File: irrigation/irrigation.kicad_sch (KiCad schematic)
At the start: 37 parts, among them J1 24V Jmp, J10 24V, J11 25%, J12 50%, J13 75%, J14 100%, J15 100%, J16 100%, J17 Pump, J2 Power, J3 Power, J4 Power, J5 Power, J6 Power, J7 Power, J8 0V Jmp, J9 Empty, K1 PLC-RPT-24DC/21, K2 PLC-RPT-24DC/21, M1 Pump, SW1 Well Empty, SW2 100% Full, SW3 25% Full, SW4 50% Full, SW5 75% Full, U1 MPPT-Charger

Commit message: Attempting to organize
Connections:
- net at J10.: now also J15.; no longer J14.
- net at J16.: now also J15.; no longer J14.
- new net: J10., J14.
- new net: J14., J16.
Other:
- note added: "Front-Panel LEDs"
- moved on the sheet: D1, D2, D3, D4, D5, D6, J10, J11, J12, J13, J14, J15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

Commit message: Organization
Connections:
- net at J10.: now also J15.; no longer J14.
- net at J16.: now also J15.; no longer J14.
- new net: J10., J14.
- new net: J14., J16.
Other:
- moved on the sheet: D1, D2, D3, D4, D5, D6, J10, J11, J12, J13, J14, J15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

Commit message: Organization
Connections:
- net at J10.: now also J15.; no longer J14.
- net at J16.: now also J15.; no longer J14.
- new net: J10., J14.
- new net: J14., J16.
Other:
- company: (none) -> Catsle
- title: (none) -> Irrigation Phase 1
- moved on the sheet: K1, K2
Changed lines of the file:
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@@
 	(generator "eeschema")
 	(generator_version "9.0")
-	(paper "A4")
+	(paper "A")
+	(title_block
+		(title "Irrigation Phase 1")
+		(date "2025-04-03")
+		(rev "1")
+		(company "Catsle")
+	)
 	(rectangle
 		(start 15.24 140.97)
@@
 	)
 	(no_connect
-		(at 187.96 60.96)
+		(at 185.42 60.96)
 	)
 	(no_connect
@@
 	(wire
 		(pts
-			(xy 142.24 140.97) (xy 151.13 140.97)
+			(xy 142.24 140.97) (xy 147.32 140.97)
 		)
 		(stroke
@@
 	(wire
 		(pts
-			(xy 227.33 64.77) (xy 246.38 64.77)
+			(xy 227.33 64.77) (xy 236.22 64.77)
 		)
 		(stroke
@@
 	(wire
 		(pts
-			(xy 227.33 152.4) (xy 246.38 152.4)
+			(xy 227.33 152.4) (xy 236.22 152.4)
 		)
 		(stroke
@@
 	(wire
 		(pts
-			(xy 110.49 29.21) (xy 208.28 29.21)
+			(xy 110.49 29.21) (xy 203.2 29.21)
 		)
 		(stroke
@@
 	(wire
 		(pts
-			(xy 227.33 97.79) (xy 246.38 97.79)
+			(xy 227.33 97.79) (xy 236.22 97.79)
 		)
 		(stroke
@@
 	(wire
 		(pts
-			(xy 227.33 81.28) (xy 246.38 81.28)
+			(xy 227.33 81.28) (xy 236.22 81.28)
 		)
 		(stroke
@@
 	(wire
 		(pts
-			(xy 166.37 143.51) (xy 170.18 143.51)
+			(xy 162.56 143.51) (xy 166.37 143.51)
 		)
 		(stroke
@@
 	(wire
 		(pts
-			(xy 187.96 55.88) (xy 208.28 55.88)
+			(xy 185.42 55.88) (xy 203.2 55.88)
 		)
 		(stroke
@@
 	(wire
 		(pts
-			(xy 170.18 58.42) (xy 172.72 58.42)
+			(xy 166.37 58.42) (xy 170.18 58.42)
 		)
 		(stroke
@@
 	(wire
 		(pts
-			(xy 227.33 138.43) (xy 246.38 138.43)
+			(xy 227.33 138.43) (xy 236.22 138.43)
 		)
 		(stroke
@@
 	(wire
 		(pts
-			(xy 110.49 48.26) (xy 172.72 48.26)
+			(xy 110.49 48.26) (xy 170.18 48.26)
 		)
 		(stroke
@@
 	(wire
 		(pts
-			(xy 204.47 152.4) (xy 219.71 152.4)
+			(xy 212.09 152.4) (xy 219.71 152.4)
 		)
 		(stroke
@@
 	(wire
 		(pts
-			(xy 110.49 130.81) (xy 151.13 130.81)
+			(xy 110.49 130.81) (xy 147.32 130.81)
 		)
 		(stroke
@@
 	(wire
 		(pts
-			(xy 187.96 48.26) (xy 194.31 48.26)
+			(xy 185.42 48.26) (xy 189.23 48.26)
 		)
 		(stroke
@@
 	(wire
 		(pts
-			(xy 166.37 130.81) (xy 176.53 130.81)
+			(xy 162.56 130.81) (xy 172.72 130.81)
 		)
 		(stroke
@@
 	(wire
 		(pts
-			(xy 208.28 29.21) (xy 208.28 55.88)
+			(xy 203.2 29.21) (xy 203.2 55.88)
 		)
 		(stroke
@@
 	(wire
 		(pts
-			(xy 227.33 114.3) (xy 246.38 114.3)
+			(xy 227.33 114.3) (xy 236.22 114.3)
 		)
 		(stroke
@@
 	(wire
 		(pts
-			(xy 170.18 58.42) (xy 170.18 143.51)
+			(xy 166.37 58.42) (xy 166.37 143.51)
 		)
 		(stroke
@@
 	(wire
 		(pts
-			(xy 166.37 138.43) (xy 219.71 138.43)
+			(xy 162.56 138.43) (xy 219.71 138.43)
 		)
 		(stroke
@@
 	)
 	(label "8"
-		(at 167.64 143.51 0)
+		(at 163.83 143.51 0)
 		(effects
 			(font
@@
 	)
 	(label "19"
-		(at 173.99 130.81 0)
+		(at 170.18 130.81 0)
 		(effects
 			(font
@@
 	)
 	(label "27"
-		(at 167.64 138.43 0)
+		(at 163.83 138.43 0)
 		(effects
 			(font
@@
 	)
 	(label "25"
-		(at 149.86 130.81 180)
+		(at 146.05 130.81 180)
 		(effects
 			(font
@@
 	)
 	(label "26"
-		(at 189.23 55.88 0)
+		(at 186.69 55.88 0)
 		(effects
 			(font
@@
 	)
 	(label "24"
-		(at 171.45 48.26 180)
+		(at 168.91 48.26 180)
 		(effects
 			(font
@@
 	)
 	(label "14"
-		(at 189.23 48.26 0)
+		(at 186.69 48.26 0)
 		(effects
 			(font
@@
 	)
 	(label "8"
-		(at 171.45 58.42 180)
+		(at 168.91 58.42 180)
 		(effects
 			(font
@@
 	)
 	(label "20"
-		(at 147.32 140.97 180)
+		(at 146.05 140.97 180)
 		(effects
 			(font
@@
 	(global_label "100% Out"
 		(shape input)
-		(at 194.31 48.26 0)
+		(at 189.23 48.26 0)
 		(fields_autoplaced yes)
 		(effects
@@
 		)
 		(property "Intersheetrefs" "${INTERSHEET_REFS}"
-			(at 206.5479 48.26 0)
+			(at 201.4679 48.26 0)
 			(effects
 				(font
@@
 	(global_label "Empty Out"
 		(shape input)
-		(at 176.53 130.81 0)
+		(at 172.72 130.81 0)
 		(fields_autoplaced yes)
 		(effects
@@
 		)
 		(property "Intersheetrefs" "${INTERSHEET_REFS}"
-			(at 189.3726 130.81 0)
+			(at 185.5626 130.81 0)
 			(effects
 				(font
@@
 	(global_label "75% Out"
 		(shape input)
-		(at 246.38 81.28 0)
+		(at 236.22 81.28 0)
 		(fields_autoplaced yes)
 		(effects
@@
 		)
 		(property "Intersheetrefs" "${INTERSHEET_REFS}"
-			(at 257.4084 81.28 0)
+			(at 247.2484 81.28 0)
 			(effects
 				(font
@@
 	(global_label "25% Out"
 		(shape input)
-		(at 246.38 114.3 0)
+		(at 236.22 114.3 0)
 		(fields_autoplaced yes)
 		(effects
@@
 		)
 		(property "Intersheetrefs" "${INTERSHEET_REFS}"
-			(at 257.4084 114.3 0)
+			(at 247.2484 114.3 0)
 			(effects
 				(font
@@
 	(global_label "50% Out"
 		(shape input)
-		(at 246.38 97.79 0)
+		(at 236.22 97.79 0)
 		(fields_autoplaced yes)
 		(effects
@@
 		)
 		(property "Intersheetrefs" "${INTERSHEET_REFS}"
-			(at 257.4084 97.79 0)
+			(at 247.2484 97.79 0)
 			(effects
 				(font
@@
 	(global_label "100% LED Out"
 		(shape input)
-		(at 246.38 64.77 0)
+		(at 236.22 64.77 0)
 		(fields_autoplaced yes)
 		(effects
@@
 		)
 		(property "Intersheetrefs" "${INTERSHEET_REFS}"
-			(at 263.0326 64.77 0)
+			(at 252.8726 64.77 0)
 			(effects
 				(font
@@
 	(global_label "Power In"
 		(shape input)
-		(at 204.47 152.4 180)
+		(at 212.09 152.4 180)
 		(fields_autoplaced yes)
 		(effects
@@
 		)
 		(property "Intersheetrefs" "${INTERSHEET_REFS}"
-			(at 193.1391 152.4 0)
+			(at 200.7591 152.4 0)
 			(effects
 				(font
@@
 	(global_label "Empty LED Out"
 		(shape input)
-		(at 246.38 138.43 0)
+		(at 236.22 138.43 0)
 		(fields_autoplaced yes)
 		(effects
@@
 		)
 		(property "Intersheetrefs" "${INTERSHEET_REFS}"
-			(at 263.6373 138.43 0)
+			(at 253.4773 138.43 0)
 			(effects
 				(font
@@
 	(global_label "Power Out"
 		(shape input)
-		(at 246.38 152.4 0)
+		(at 236.22 152.4 0)
 		(fields_autoplaced yes)
 		(effects
@@
 		)
 		(property "Intersheetrefs" "${INTERSHEET_REFS}"
-			(at 259.1623 152.4 0)
+			(at 249.0023 152.4 0)
 			(effects
 				(font
@@
 	(symbol
 		(lib_id "Phoenix Contact:PLC-RPT-24DC/21")
-		(at 180.34 53.34 270)
+		(at 177.8 53.34 270)
 		(unit 1)
 		(exclude_from_sim no)
@@
 		(fields_autoplaced yes)
 		(property "Reference" "K2"
-			(at 180.34 38.1 90)
+			(at 177.8 38.1 90)
 			(effects
 				(font
@@
 		)
 		(property "Value" "PLC-RPT-24DC/21"
-			(at 180.34 40.64 90)
+			(at 177.8 40.64 90)
 			(effects
 				(font
@@
 		)
 		(property "Footprint" ""
-			(at 179.324 82.296 0)
+			(at 176.784 82.296 0)
 			(effects
 				(font
@@
 		)
 		(property "Datasheet" "https://www.mouser.com/ProductDetail/Phoenix-Contact/2900299?qs=yDWYzLgaxI2Ztu%2F0JMLp4g%3D%3D"
-			(at 180.34 53.34 0)
+			(at 177.8 53.34 0)
 			(effects
 				(font
@@
 		)
 		(property "Description" "PLC-RPT- 24DC/21 - Relay module"
-			(at 180.34 53.34 0)
+			(at 177.8 53.34 0)
 			(effects
 				(font
@@
 	(symbol
 		(lib_id "Phoenix Contact:PLC-RPT-24DC/21")
-		(at 158.75 135.89 270)
+		(at 154.94 135.89 270)
 		(unit 1)
 		(exclude_from_sim no)
@@
 		(fields_autoplaced yes)
 		(property "Reference" "K1"
-			(at 158.75 120.65 90)
+			(at 154.94 120.65 90)
 			(effects
 				(font
@@
 		)
 		(property "Value" "PLC-RPT-24DC/21"
-			(at 158.75 123.19 90)
+			(at 154.94 123.19 90)
 			(effects
 				(font
@@
 		)
 		(property "Footprint" ""
-			(at 157.734 164.846 0)
+			(at 153.924 164.846 0)
 			(effects
 				(font
@@
 		)
 		(property "Datasheet" "https://www.mouser.com/ProductDetail/Phoenix-Contact/2900299?qs=yDWYzLgaxI2Ztu%2F0JMLp4g%3D%3D"
-			(at 158.75 135.89 0)
+			(at 154.94 135.89 0)
 			(effects
 				(font
@@
 		)
 		(property "Description" "PLC-RPT- 24DC/21 - Relay module"
-			(at 158.75 135.89 0)
+			(at 154.94 135.89 0)
 			(effects
 				(font

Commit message: Organized.
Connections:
- net 8 is gone; now on net Empty Out: K1.14, K2.11
- net at J10.: now also J15.; no longer J14.
- net at J16.: now also J15.; no longer J14.
- new net: J10., J14.
- new net: J14., J16.
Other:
- note added: "Pump Control"
- moved on the sheet: D1, D2, D3, D4, D5, D6, K1, K2

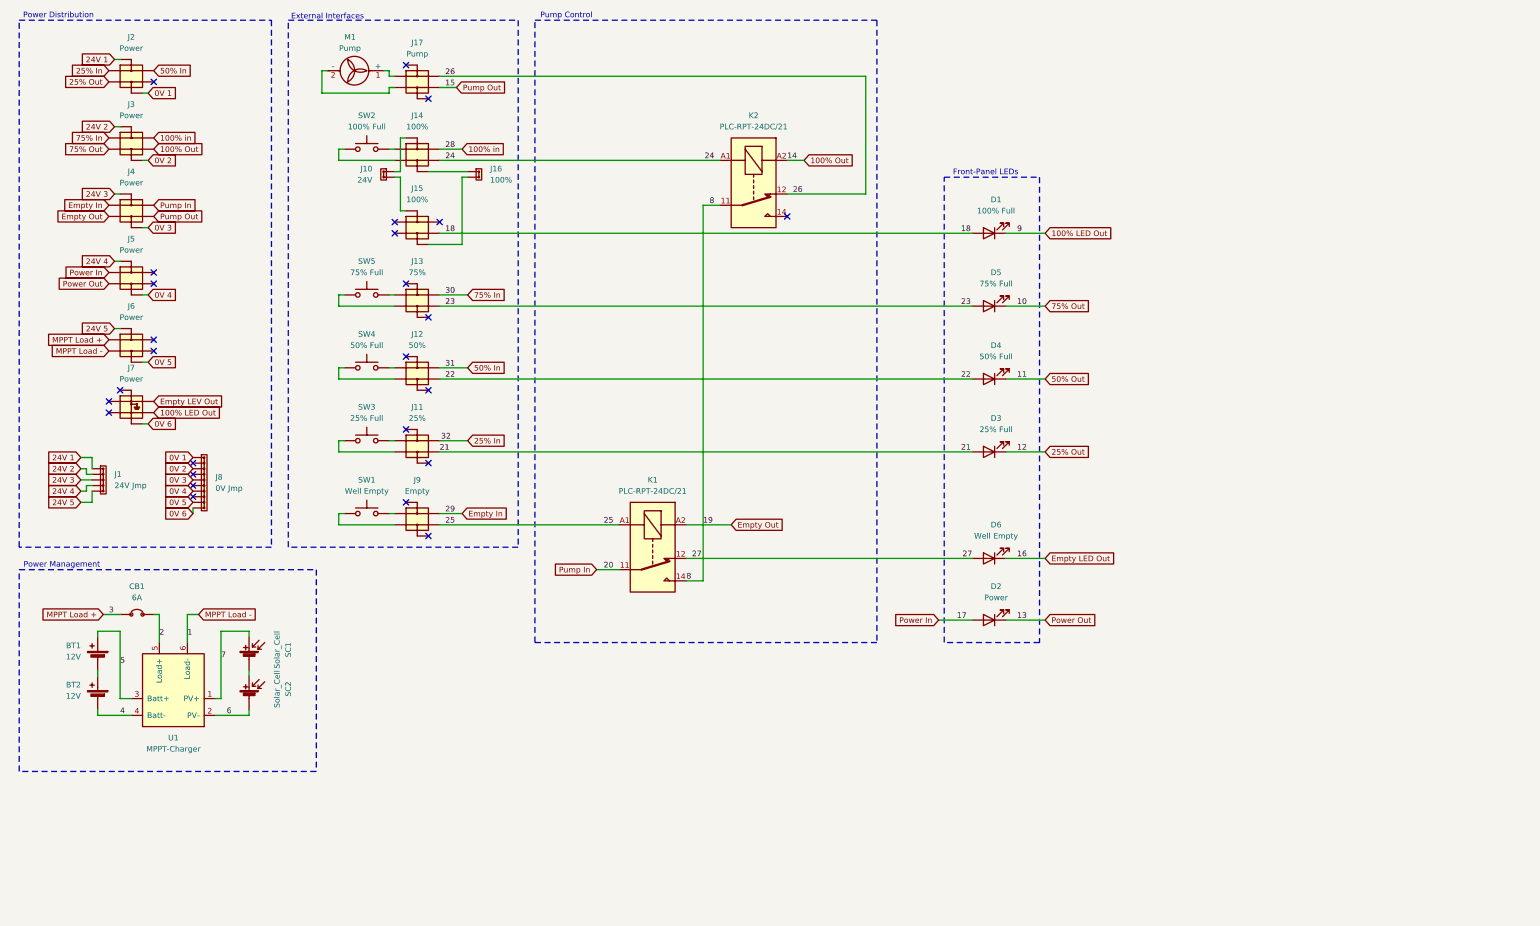
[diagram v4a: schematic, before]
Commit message: Working on adding switches and another pump
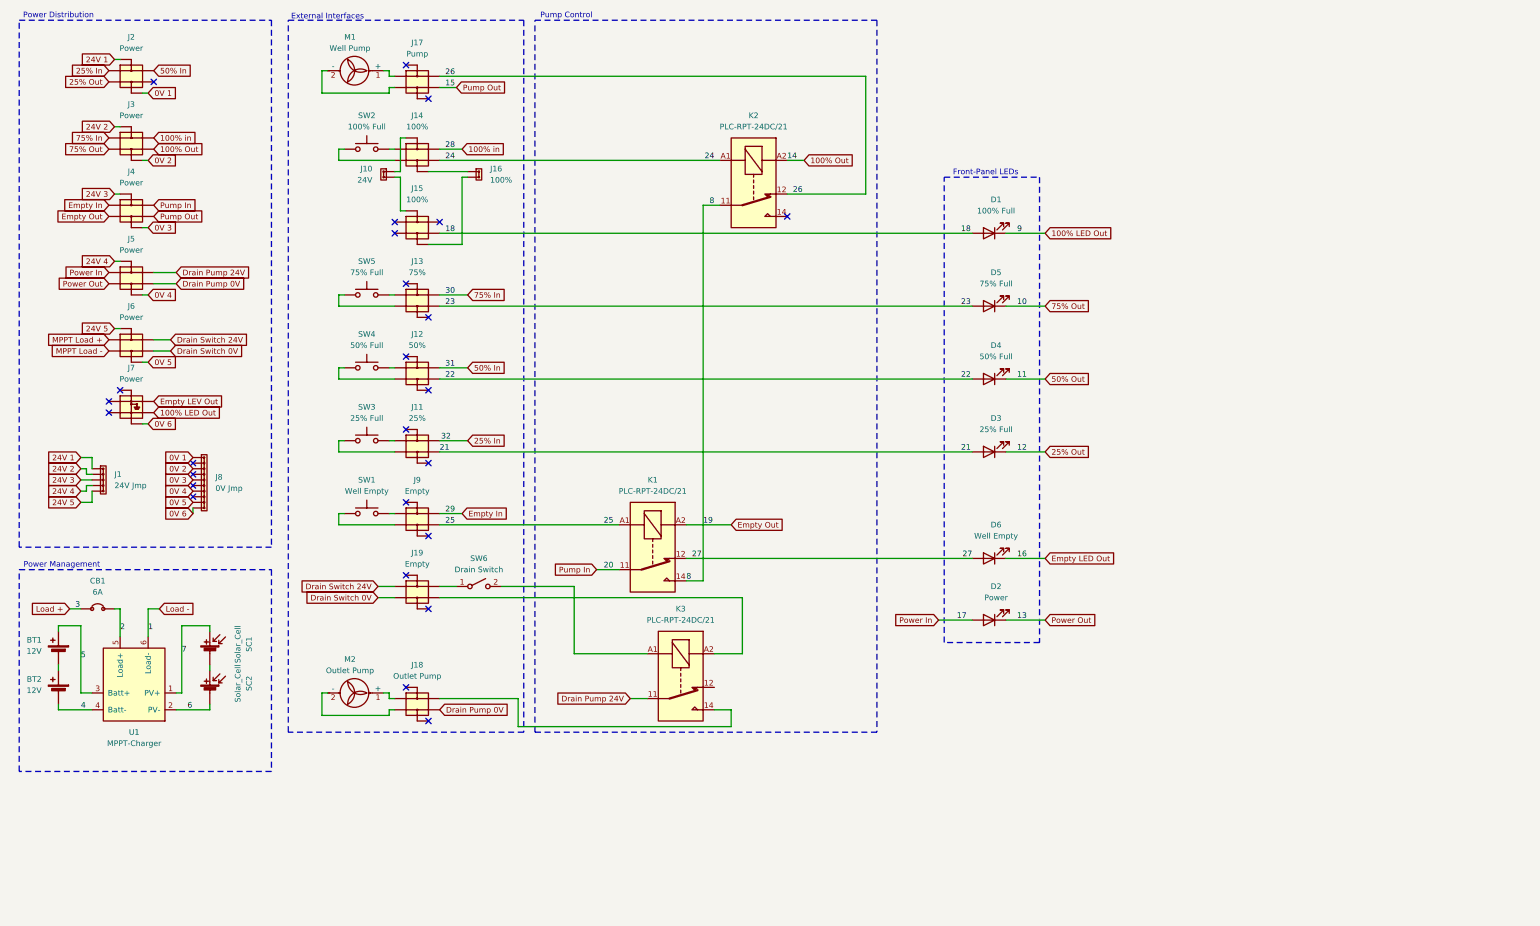
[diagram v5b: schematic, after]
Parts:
- added J18: Outlet Pump, symbol Phoenix Contact:PTTB_2,5-L/N_3210994
- added J19: Empty, symbol Phoenix Contact:PTTB_2,5-L/N_3210994
- added K3: PLC-RPT-24DC/21, symbol Phoenix Contact:PLC-RPT-24DC/21
- added M2: Outlet Pump, symbol Irrigation:Pump
- added SW6: Drain Switch, symbol Irrigation:Toggle Switch
- M1: value Pump -> Well Pump
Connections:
- net MPPT Load +: no longer CB1.
- net MPPT Load -: no longer U1.6 (Load-)
- net at J10.: now also J15.; no longer J14.
- net at J16.: now also J15.; no longer J14.
- new net: J10., J14.
- new net: J14., J16.
- new net: J18., K3.14
- new net: K3.A1, SW6.2 (B)
- new net: J19., K3.A2
- new net: J18., M2.1 (+)
- new net: J18., M2.2 (-)
- new net: J19., SW6.1 (A)
- new net Drain Pump 0V: J18., J5.
- new net Drain Pump 24V: J5., K3.11
- new net Drain Switch 0V: J19., J6.
- new net Drain Switch 24V: J19., J6.
- new net Load +: CB1.
- new net Load -: U1.6 (Load-)
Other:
- moved on the sheet: BT1, BT2, CB1, SC1, SC2, U1

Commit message: More switch?
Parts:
- added SW7: Fill Switch, symbol Irrigation:Toggle Switch
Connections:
- net 25: now also SW7.1 (A); no longer K1.A1
- net at J10.: now also J15.; no longer J14.
- net at J16.: now also J15.; no longer J14.
- new net: J10., J14.
- new net: J14., J16.
- new net: K1.A1, SW7.2 (B)
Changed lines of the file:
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@@
 	)
 	(rectangle
-		(start 15.24 140.97)
-		(end 72.39 186.69)
+		(start 15.24 138.43)
+		(end 72.39 184.15)
 		(stroke
 			(width 0)
@@
 	(text "Power Distribution"
 		(exclude_from_sim no)
-		(at 24.13 15.494 0)
+		(at 24.638 18.288 0)
 		(effects
 			(font
@@
 	(text "Pump Control"
 		(exclude_from_sim no)
-		(at 139.192 15.494 0)
+		(at 139.7 18.542 0)
 		(effects
 			(font
@@
 	(text "Front-Panel LEDs"
 		(exclude_from_sim no)
-		(at 234.188 51.054 0)
+		(at 233.934 53.848 0)
 		(effects
 			(font
@@
 	(text "External Interfaces"
 		(exclude_from_sim no)
-		(at 85.09 15.748 0)
+		(at 85.852 18.542 0)
 		(effects
 			(font
@@
 	(wire
 		(pts
+			(xy 147.32 130.81) (xy 151.13 130.81)
+		)
+		(stroke
+			(width 0)
+			(type default)
+		)
+	)
+	(wire
+		(pts
 			(xy 110.49 45.72) (xy 115.57 45.72)
 		)
@@
 	(wire
 		(pts
-			(xy 110.49 130.81) (xy 151.13 130.81)
-		)
-		(stroke
-			(width 0)
-			(type default)
-		)
-	)
-	(wire
-		(pts
 			(xy 110.49 81.28) (xy 231.14 81.28)
 		)
@@
 	(wire
 		(pts
+			(xy 110.49 130.81) (xy 137.16 130.81)
+		)
+		(stroke
+			(width 0)
+			(type default)
+		)
+	)
+	(wire
+		(pts
 			(xy 101.6 43.18) (xy 102.87 43.18)
 		)
@@
 		)
 	)
-	(label "25"
-		(at 149.86 130.81 180)
-		(effects
-			(font
-				(size 1.27 1.27)
-			)
-			(justify right bottom)
-		)
-	)
 	(label "22"
 		(at 228.6 97.79 0)
@@
 					(unit 1)
 				)
+			)
+		)
+	)
+	(symbol
+		(lib_id "Irrigation:Toggle Switch")
+		(at 142.24 130.81 0)
+		(unit 1)
+		(exclude_from_sim no)
+		(in_bom yes)
+		(on_board yes)
+		(dnp no)
+		(fields_autoplaced yes)
+		(property "Reference" "SW7"
+			(at 142.24 124.46 0)
+			(effects
+				(font
+					(size 1.27 1.27)
+				)
+			)
+		)
+		(property "Value" "Fill Switch"
+			(at 142.24 127 0)
+			(effects
+				(font
+					(size 1.27 1.27)
+				)
+			)
+		)
+		(property "Footprint" ""
+			(at 142.24 130.81 0)
+			(effects
+				(font
+					(size 1.27 1.27)
+				)
+				(hide yes)
+			)
+		)
+		(property "Datasheet" "https://www.mouser.com/ProductDetail/TE-Connectivity-Kissling/07-1-2-13-910?qs=OlC7AqGiEDn5ZAFZ0c7jmA%3D%3D"
+			(at 142.24 130.81 0)
+			(effects
+				(font
+					(size 1.27 1.27)
+				)
+				(hide yes)
+			)
+		)
+		(property "Description" "Single Pole Single Throw (SPST) switch"
+			(at 142.24 130.81 0)
+			(effects
+				(font
+					(size 1.27 1.27)
+				)
+				(hide yes)
+			)
+		)
+		(pin "2"
+		)
+		(pin "1"
+		)
+		(instances
+			(project "irrigation"
+				(path "/e99b2683-5fc9-4ee4-bdcd-d6e5faee292b"
+					(reference "SW7")
+					(unit 1)
+				)

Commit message: Layout updates
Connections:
- net at J10.: now also J15.; no longer J14.
- net at J16.: now also J15.; no longer J14.
- new net: J10., J14.
- new net: J14., J16.
- no-connect marks 26 -> 27
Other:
- moved on the sheet: D1, D2, D3, D4, D5, D6, J18, K1, K2, K3, M2, SW7
